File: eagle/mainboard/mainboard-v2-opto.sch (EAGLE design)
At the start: 64 parts, among them K1 TQ2-SA-12V, K2 TQ2-SA-12V, K3 TQ2-SA-12V, K4 TQ2-SA-12V, K5 TQ2-SA-12V, K6 TQ2-SA-12V, K7 TQ2-SA-12V, K8 TQ2-SA-12V, Q1 RS485-ADAPTER0.05-CONNECTOR

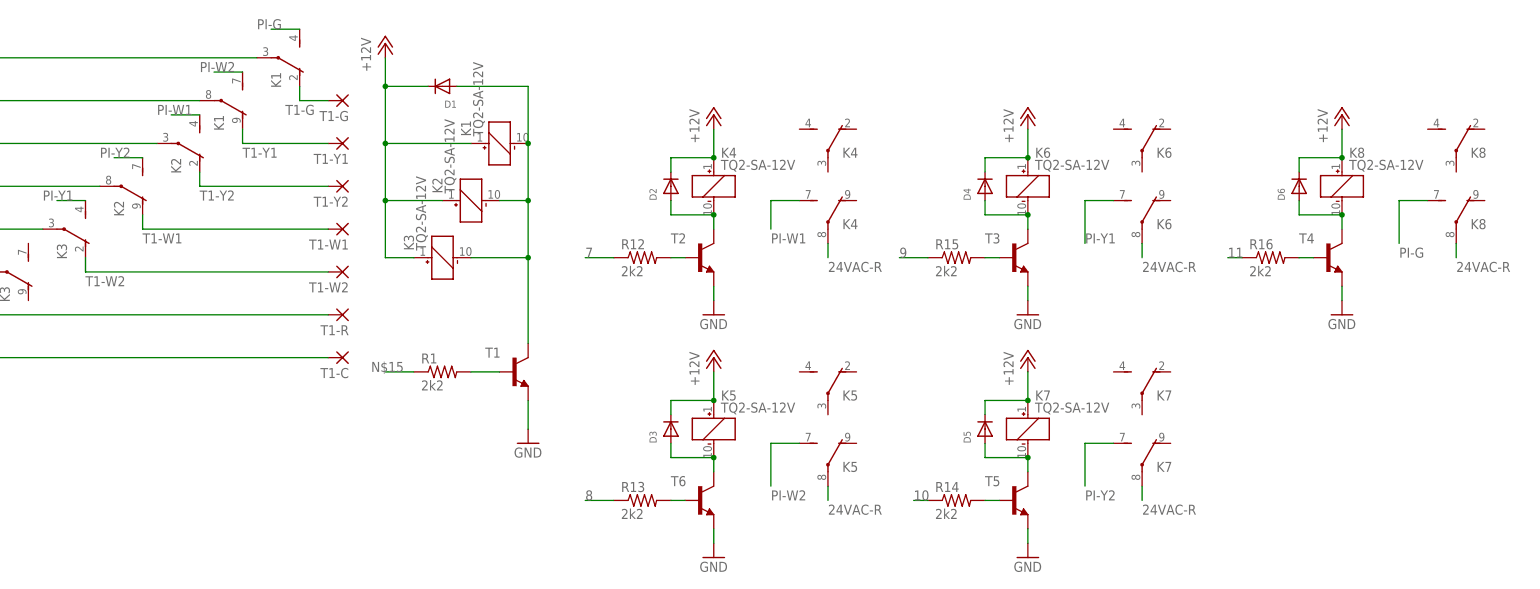
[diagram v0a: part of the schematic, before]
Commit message: Starting work on solid state relay version of mainboard, as it's much more manageable (albeit still painful)
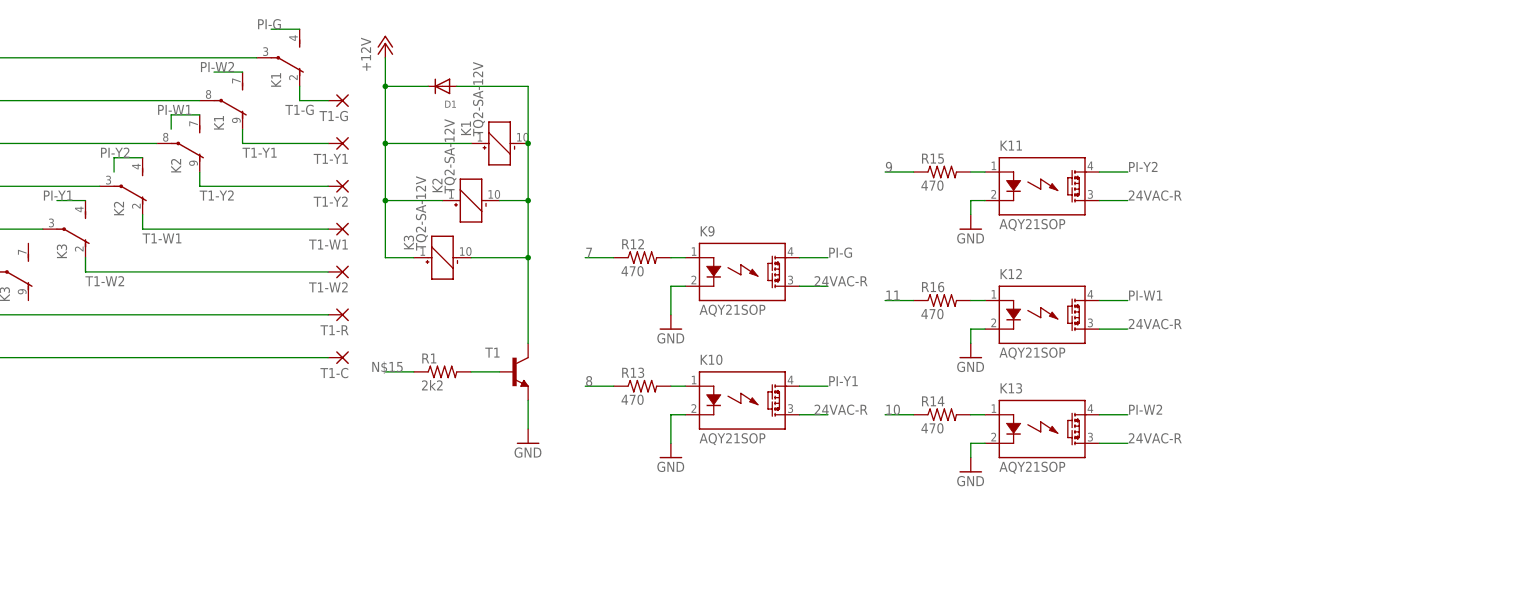
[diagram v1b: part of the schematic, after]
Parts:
- removed D2, D3, D4, D5, D6: (no value), adafruit:DIODESMA
- removed K4, K5, K6, K7, K8: TQ2-SA-12V, relay:TQ2-SA-12V
- removed T2, T3, T4, T5, T6: (no value), transistor:BC808-NPN-SOT23-BEC
- added K10, K11, K12, K13, K9: AQY21SOP, relay:AQY21SOP
- R12, R13, R14, R15, R16: value 2k2 -> 470
- T1-C, T1-G, T1-R, T1-W1, T1-W2, T1-Y1, T1-Y2, UNIT-C, UNIT-G, UNIT-R, UNIT-W1, UNIT-W2, UNIT-Y1, UNIT-Y2: device wirepad:1,6/0,9 -> wirepad:2,15/1,0
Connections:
- removed net N$21: D2.A, K4_.-, T2.C
- removed net N$25: D3.A, K5_.-, T6.C
- removed net N$26: D5.A, K7_.-, T5.C
- removed net N$28: D4.A, K6_.-, T3.C
- removed net N$31: D6.A, K8_.-, T4.C
- removed net N$33: R12.2, T2.B
- removed net N$36: R15.2, T3.B
- removed net N$38: R14.2, T5.B
- removed net N$40: R16.2, T4.B
- new net N$11: K12.A, R16.2
- new net N$12: K11.A, R15.2
- new net N$16: K9.A, R12.2
- new net N$8: K13.A, R14.2
- net +12V: no longer D2.C, D3.C, D4.C, D5.C, D6.C, K4_.+, K5_.+, K6_.+, K7_.+, K8_.+
- net 24VAC-R: now also K10.DS2, K11.DS2, K12.DS2, K13.DS2, K9.DS2; no longer K42.P, K52.P, K62.P, K72.P, K82.P
- net GND: now also K10.K, K11.K, K12.K, K13.K, K9.K; no longer T2.E, T3.E, T4.E, T5.E, T6.E
- net N$32: no longer T6.B
- net N$4: now also K22.P; no longer K21.P
- net N$7: now also K21.P; no longer K22.P
- net PI-G: now also K9.DS1; no longer K82.S
- net PI-W1: now also K12.DS1, K22.S; no longer K21.S, K42.S
- net PI-W2: now also K13.DS1; no longer K52.S
- net PI-Y1: now also K10.DS1; no longer K62.S
- net PI-Y2: now also K11.DS1, K21.S; no longer K22.S, K72.S
- net T1-W1: now also K21.O; no longer K22.O
- net T1-Y2: now also K22.O; no longer K21.O
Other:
- moved on the sheet: K2, R13, R14, R15, R16

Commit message: Really close to finishing first prototype of the motherboard.
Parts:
- added I2C: (no value), con-amp-quick:M04
- added U$2: SWITCH-1, serge:SWITCH-1
- renumbered SL1 to RS1
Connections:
- net N$19 renamed RS-12V
- net N$23 renamed RS-A
- net N$24 renamed RS-B
- removed net 24: R11.1, R7.2
- removed net N$32: R13.2
- new net 25: R14.1, U$1.25
- new net 27: R4.2, R8.1, U$1.27
- new net N$17: K10.A, R13.2
- new net SDA: I2C.2, U$1.2(SDA)
- new net SLC: I2C.3, U$1.3(SLC)
- net +5V: now also I2C.1
- net 10: now also R1.1, U$1.10; no longer R14.1
- net 11: now also U$1.11
- net 17: now also R10.1, R6.2, U$1.17; no longer R2.2, R3.1
- net 18: now also R5.2, R9.1, U$1.18; no longer R4.2, R8.1
- net 22: now also R2.2, R3.1, U$1.22; no longer R5.2, R9.1
- net 23: now also R11.1, R7.2, U$1.23; no longer R10.1, R6.2
- net 7: now also U$1.7
- net 8: now also U$1.8
- net 9: now also U$1.9
- net GND: now also I2C.4, U$2.P; no longer T1.E
- net N$15: now also T1.E, U$2.S; no longer R1.1
